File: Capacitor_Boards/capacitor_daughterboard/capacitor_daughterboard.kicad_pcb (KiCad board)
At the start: 2 copper layers, 33 x 32 mm, 5 parts, among them P1 Conn_01x02_Male, P2 Conn_01x02_Male

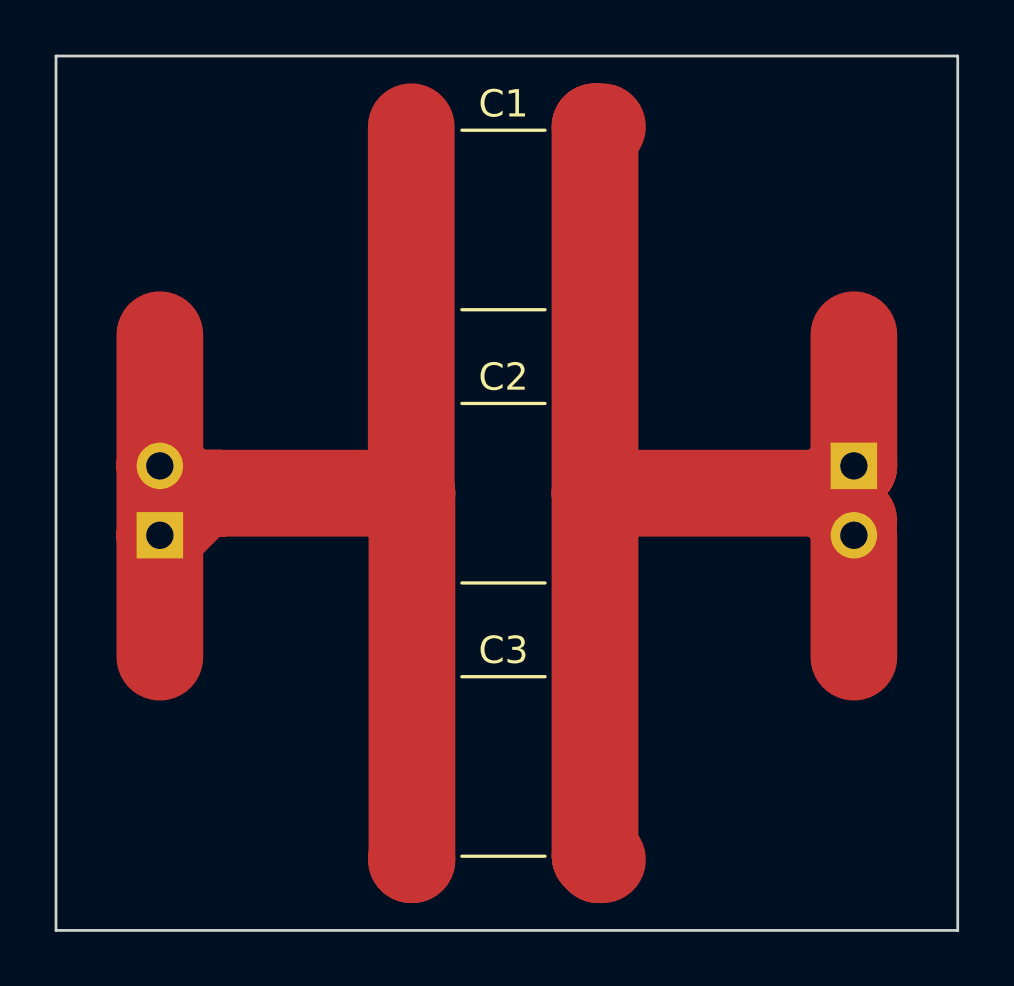
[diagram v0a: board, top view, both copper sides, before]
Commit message: resized capacitor daughterboard to have just 2 caps.
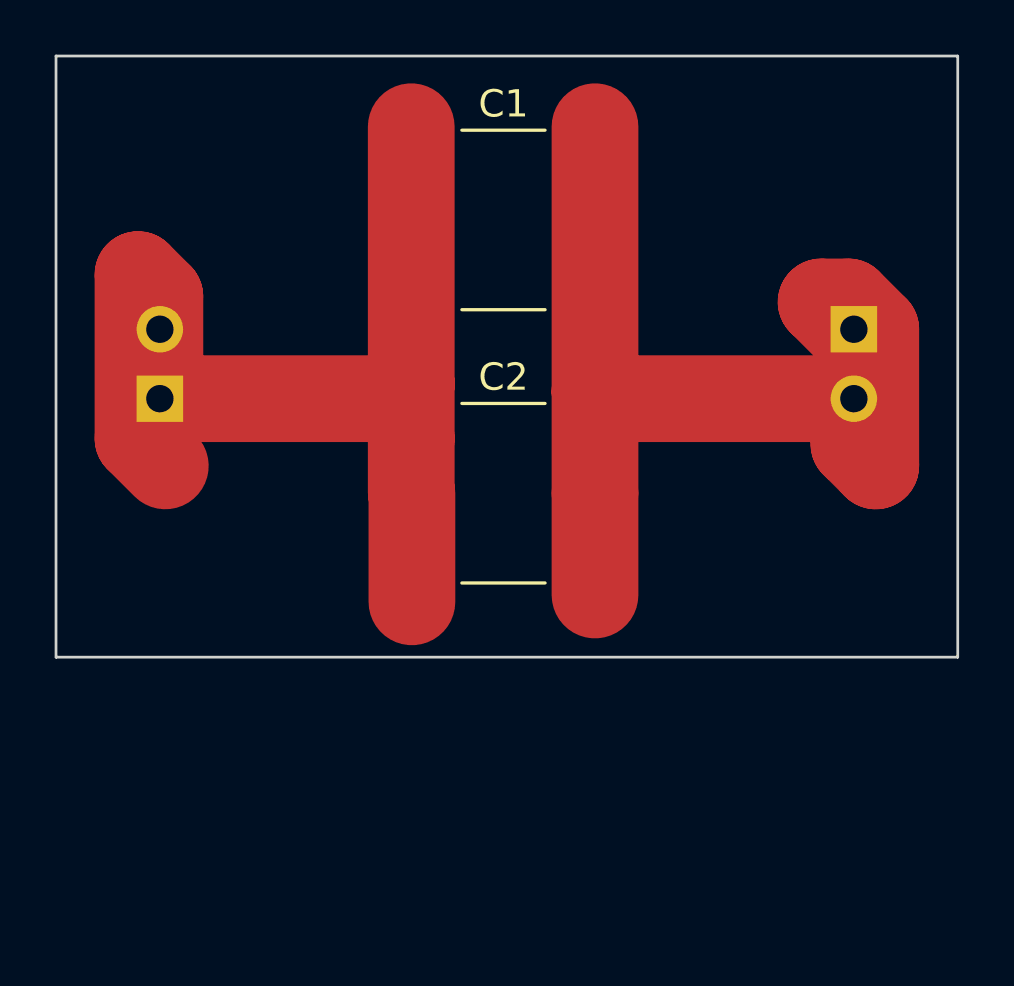
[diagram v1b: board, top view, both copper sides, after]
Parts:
- removed C3: C, Capacitor_SMD:C_2225_5664Metric_Pad1.80x6.60mm_HandSolder
- moved J1 5.00 mm to (127.8, 81.5)
- moved J2 5.00 mm to (153.2, 79.0)
- renumbered P1 to J1, P2 to J2
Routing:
- net Net-(C1-Pad1): track 53.1 -> 39.1 mm
- net Net-(C1-Pad2): track 47.9 -> 38.5 mm
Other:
- board size 33 x 32 mm -> 33 x 22 mm
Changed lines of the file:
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@@
   (net 2 "Net-(C1-Pad2)")
-  (footprint "Capacitor_SMD:C_2225_5664Metric_Pad1.80x6.60mm_HandSolder" (layer "F.Cu")
-    (at 140.375 95)
-    (descr "Capacitor SMD 2225 (5664 Metric), square (rectangular) end terminal, IPC_7351 nominal with elongated pad for handsoldering. (Body size from: http://datasheets.avx.com/AVX-HV_MLCC.pdf), generated with kicad-footprint-generator")
-    (tags "capacitor handsolder")
-    (property "Sheetfile" "capacitor_daughterboard.kicad_sch")
-    (property "Sheetname" "")
-    (attr smd)
-    (fp_text reference "C3" (at 0 -4.25) (layer "F.SilkS")
-      (effects (font (size 1 1) (thickness 0.15)))
-    )
-    (fp_text value "C" (at 0 4.25) (layer "F.Fab")
-      (effects (font (size 1 1) (thickness 0.15)))
-    )
-    (fp_text user "${REFERENCE}" (at 0 0) (layer "F.Fab")
-      (effects (font (size 1 1) (thickness 0.15)))
-    )
-    (fp_line (start -1.522369 -3.285) (end 1.522369 -3.285) (layer "F.SilkS") (width 0.12))
-    (fp_line (start -1.522369 3.285) (end 1.522369 3.285) (layer "F.SilkS") (width 0.12))
-    (fp_line (start 3.78 3.55) (end -3.78 3.55) (layer "F.CrtYd") (width 0.05))
-    (fp_line (start -3.78 -3.55) (end 3.78 -3.55) (layer "F.CrtYd") (width 0.05))
-    (fp_line (start 3.78 -3.55) (end 3.78 3.55) (layer "F.CrtYd") (width 0.05))
-    (fp_line (start -3.78 3.55) (end -3.78 -3.55) (layer "F.CrtYd") (width 0.05))
-    (fp_line (start 2.86 -3.175) (end 2.86 3.175) (layer "F.Fab") (width 0.1))
-    (fp_line (start 2.86 3.175) (end -2.86 3.175) (layer "F.Fab") (width 0.1))
-    (fp_line (start -2.86 3.175) (end -2.86 -3.175) (layer "F.Fab") (width 0.1))
-    (fp_line (start -2.86 -3.175) (end 2.86 -3.175) (layer "F.Fab") (width 0.1))
-    (pad "1" smd roundrect (at -3.35 0) (size 2.8 7) (layers "F.Cu" "F.Paste" "F.Mask") (roundrect_rratio 0.138889)
-      (net 1 "Net-(C1-Pad1)") (pintype "passive"))
-    (pad "2" smd roundrect (at 3.35 0) (size 2.8 7) (layers "F.Cu" "F.Paste" "F.Mask") (roundrect_rratio 0.138889)
-      (net 2 "Net-(C1-Pad2)") (pintype "passive"))
-    (model "${KICAD6_3DMODEL_DIR}/Capacitor_SMD.3dshapes/C_2225_5664Metric.wrl"
-      (offset (xyz 0 0 0))
-      (scale (xyz 1 1 1))
-      (rotate (xyz 0 0 0))
-    )
-  )
   (footprint "Capacitor_SMD:C_2225_5664Metric_Pad1.80x6.60mm_HandSolder" (layer "F.Cu")
     (at 140.375 85)
@@
   )
   (footprint "Connector_PinHeader_2.54mm:PinHeader_1x02_P2.54mm_Vertical" (layer "B.Cu")
-    (at 153.19939 84 180)
+    (at 153.19939 79 180)
     (descr "Through hole straight pin header, 1x02, 2.54mm pitch, single row")
     (tags "Through hole pin header THT 1x02 2.54mm single row")
@@
     (property "Sheetname" "")
     (attr through_hole)
-    (fp_text reference "P2" (at 0 -5) (layer "B.SilkS")
+    (fp_text reference "J2" (at 0 -5) (layer "B.SilkS")
       (effects (font (size 1 1) (thickness 0.15)) (justify mirror))
     )
@@
   )
   (footprint "Connector_PinHeader_2.54mm:PinHeader_1x02_P2.54mm_Vertical" (layer "B.Cu")
-    (at 127.80061 86.54)
+    (at 127.80061 81.54)
     (descr "Through hole straight pin header, 1x02, 2.54mm pitch, single row")
     (tags "Through hole pin header THT 1x02 2.54mm single row")
@@
     (property "Sheetname" "")
     (attr through_hole)
-    (fp_text reference "P1" (at 0 2.33) (layer "B.SilkS")
+    (fp_text reference "J1" (at 0 2.33) (layer "B.SilkS")
       (effects (font (size 1 1) (thickness 0.15)) (justify mirror))
     )
@@
     )
   )
-  (gr_rect (start 124 69) (end 157 101) (layer "Edge.Cuts") (width 0.1) (fill none))
-  (segment (start 127.80061 86.54) (end 127.80061 84) (width 3.175) (layer "F.Cu") (net 1))
-  (segment (start 130 85) (end 128 85) (width 3.175) (layer "F.Cu") (net 1))
-  (segment (start 137.025 98.41248) (end 137 98.41248) (width 3.175) (layer "F.Cu") (net 1))
-  (segment (start 130 85) (end 129.34061 85) (width 3.175) (layer "F.Cu") (net 1))
-  (segment (start 137 84.975) (end 137.025 85) (width 3.175) (layer "F.Cu") (net 1))
-  (segment (start 127.80061 86.54) (end 127.80061 91) (width 3.175) (layer "F.Cu") (net 1))
-  (segment (start 127.80061 84) (end 127.80061 79.19939) (width 3.175) (layer "F.Cu") (net 1))
-  (segment (start 128.80061 85) (end 127.80061 84) (width 3.175) (layer "F.Cu") (net 1))
-  (segment (start 130 85) (end 137.025 85) (width 3.175) (layer "F.Cu") (net 1))
-  (segment (start 129.34061 85) (end 127.80061 86.54) (width 3.175) (layer "F.Cu") (net 1))
-  (segment (start 130 85) (end 128.80061 85) (width 3.175) (layer "F.Cu") (net 1))
-  (segment (start 137.025 85) (end 137.025 98.41248) (width 3.175) (layer "F.Cu") (net 1))
-  (segment (start 137 71.58752) (end 137 84.975) (width 3.175) (layer "F.Cu") (net 1))
-  (segment (start 143.725 85) (end 143.725 98.275) (width 3.175) (layer "F.Cu") (net 2))
-  (segment (start 153.19939 86.54) (end 153.19939 91) (width 3.175) (layer "F.Cu") (net 2))
-  (segment (start 143.86248 98.41248) (end 144 98.41248) (width 3.175) (layer "F.Cu") (net 2))
-  (segment (start 152.19939 85) (end 153.19939 86) (width 3.175) (layer "F.Cu") (net 2))
-  (segment (start 152.19939 85) (end 153.19939 84) (width 3.175) (layer "F.Cu") (net 2))
-  (segment (start 153.19939 79.19939) (end 153.19939 84) (width 3.175) (layer "F.Cu") (net 2))
-  (segment (start 143.725 85) (end 143.725 71.58752) (width 3.175) (layer "F.Cu") (net 2))
-  (segment (start 143.725 98.275) (end 143.86248 98.41248) (width 3.175) (layer "F.Cu") (net 2))
-  (segment (start 143.725 71.58752) (end 144 71.58752) (width 3.175) (layer "F.Cu") (net 2))
-  (segment (start 152.19939 85) (end 143.725 85) (width 3.175) (layer "F.Cu") (net 2))
+  (gr_rect (start 124 69) (end 157 91) (layer "Edge.Cuts") (width 0.1) (fill none))
+  (segment (start 137 83) (end 137 84.975) (width 3.175) (layer "F.Cu") (net 1))
+  (segment (start 137 81) (end 137 83) (width 3.175) (layer "F.Cu") (net 1))
+  (segment (start 127 83) (end 128 84) (width 3.175) (layer "F.Cu") (net 1))
+  (segment (start 127 77) (end 127 83) (width 3.175) (layer "F.Cu") (net 1))
+  (segment (start 137 71.58752) (end 137 81) (width 3.175) (layer "F.Cu") (net 1))
+  (segment (start 127.80061 81.54) (end 136.46 81.54) (width 3.175) (layer "F.Cu") (net 1))
+  (segment (start 137.025 85) (end 137.025 88.975) (width 3.175) (layer "F.Cu") (net 1))
+  (segment (start 127.80061 77.80061) (end 127 77) (width 3.175) (layer "F.Cu") (net 1))
+  (segment (start 127.80061 81.54) (end 127.80061 77.80061) (width 3.175) (layer "F.Cu") (net 1))
+  (segment (start 136.46 81.54) (end 137 81) (width 3.175) (layer "F.Cu") (net 1))
+  (segment (start 154 84) (end 154 79) (width 3.175) (layer "F.Cu") (net 2))
+  (segment (start 153.19939 81.54) (end 143.99 81.54) (width 3.175) (layer "F.Cu") (net 2))
+  (segment (start 153 78) (end 154 79) (width 3.175) (layer "F.Cu") (net 2))
+  (segment (start 143.725 85) (end 143.725 88.725) (width 3.175) (layer "F.Cu") (net 2))
+  (segment (start 153.19939 83.19939) (end 154 84) (width 3.175) (layer "F.Cu") (net 2))
+  (segment (start 153.19939 79) (end 153 79) (width 3.175) (layer "F.Cu") (net 2))
+  (segment (start 153 79) (end 152 78) (width 3.175) (layer "F.Cu") (net 2))
+  (segment (start 143.725 85) (end 143.725 81.275) (width 3.175) (layer "F.Cu") (net 2))
+  (segment (start 153.19939 81.54) (end 153.19939 83.19939) (width 3.175) (layer "F.Cu") (net 2))
+  (segment (start 143.725 81.275) (end 143.725 71.58752) (width 3.175) (layer "F.Cu") (net 2))
+  (segment (start 152 78) (end 153 78) (width 3.175) (layer "F.Cu") (net 2))
+  (segment (start 143.99 81.54) (end 143.725 81.275) (width 3.175) (layer "F.Cu") (net 2))
 )

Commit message: Connected the QLA  connector
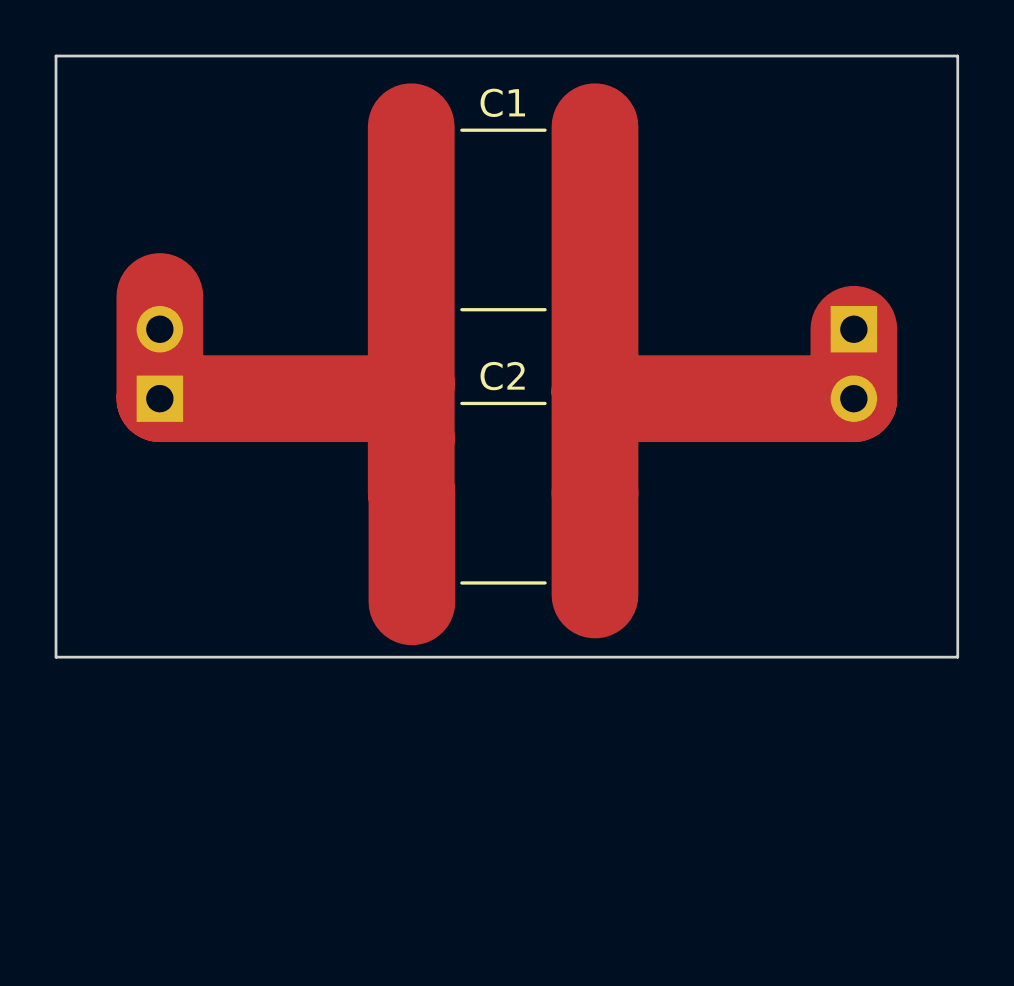
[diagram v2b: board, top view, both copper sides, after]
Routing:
- net Net-(C1-Pad2): track 38.5 -> 29.3 mm
- net Net-(C1-Pad1): track 39.1 -> 30.5 mm
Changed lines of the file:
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@@
   (segment (start 137 83) (end 137 84.975) (width 3.175) (layer "F.Cu") (net 1))
   (segment (start 137 81) (end 137 83) (width 3.175) (layer "F.Cu") (net 1))
-  (segment (start 127 83) (end 128 84) (width 3.175) (layer "F.Cu") (net 1))
-  (segment (start 127 77) (end 127 83) (width 3.175) (layer "F.Cu") (net 1))
   (segment (start 137 71.58752) (end 137 81) (width 3.175) (layer "F.Cu") (net 1))
   (segment (start 127.80061 81.54) (end 136.46 81.54) (width 3.175) (layer "F.Cu") (net 1))
   (segment (start 137.025 85) (end 137.025 88.975) (width 3.175) (layer "F.Cu") (net 1))
-  (segment (start 127.80061 77.80061) (end 127 77) (width 3.175) (layer "F.Cu") (net 1))
   (segment (start 127.80061 81.54) (end 127.80061 77.80061) (width 3.175) (layer "F.Cu") (net 1))
   (segment (start 136.46 81.54) (end 137 81) (width 3.175) (layer "F.Cu") (net 1))
-  (segment (start 154 84) (end 154 79) (width 3.175) (layer "F.Cu") (net 2))
   (segment (start 153.19939 81.54) (end 143.99 81.54) (width 3.175) (layer "F.Cu") (net 2))
-  (segment (start 153 78) (end 154 79) (width 3.175) (layer "F.Cu") (net 2))
   (segment (start 143.725 85) (end 143.725 88.725) (width 3.175) (layer "F.Cu") (net 2))
-  (segment (start 153.19939 83.19939) (end 154 84) (width 3.175) (layer "F.Cu") (net 2))
-  (segment (start 153.19939 79) (end 153 79) (width 3.175) (layer "F.Cu") (net 2))
-  (segment (start 153 79) (end 152 78) (width 3.175) (layer "F.Cu") (net 2))
   (segment (start 143.725 85) (end 143.725 81.275) (width 3.175) (layer "F.Cu") (net 2))
-  (segment (start 153.19939 81.54) (end 153.19939 83.19939) (width 3.175) (layer "F.Cu") (net 2))
   (segment (start 143.725 81.275) (end 143.725 71.58752) (width 3.175) (layer "F.Cu") (net 2))
-  (segment (start 152 78) (end 153 78) (width 3.175) (layer "F.Cu") (net 2))
   (segment (start 143.99 81.54) (end 143.725 81.275) (width 3.175) (layer "F.Cu") (net 2))
+  (segment (start 153.19939 81.54) (end 153.19939 79) (width 3.175) (layer "F.Cu") (net 2))
 )

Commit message: Shrunk Daughter Board
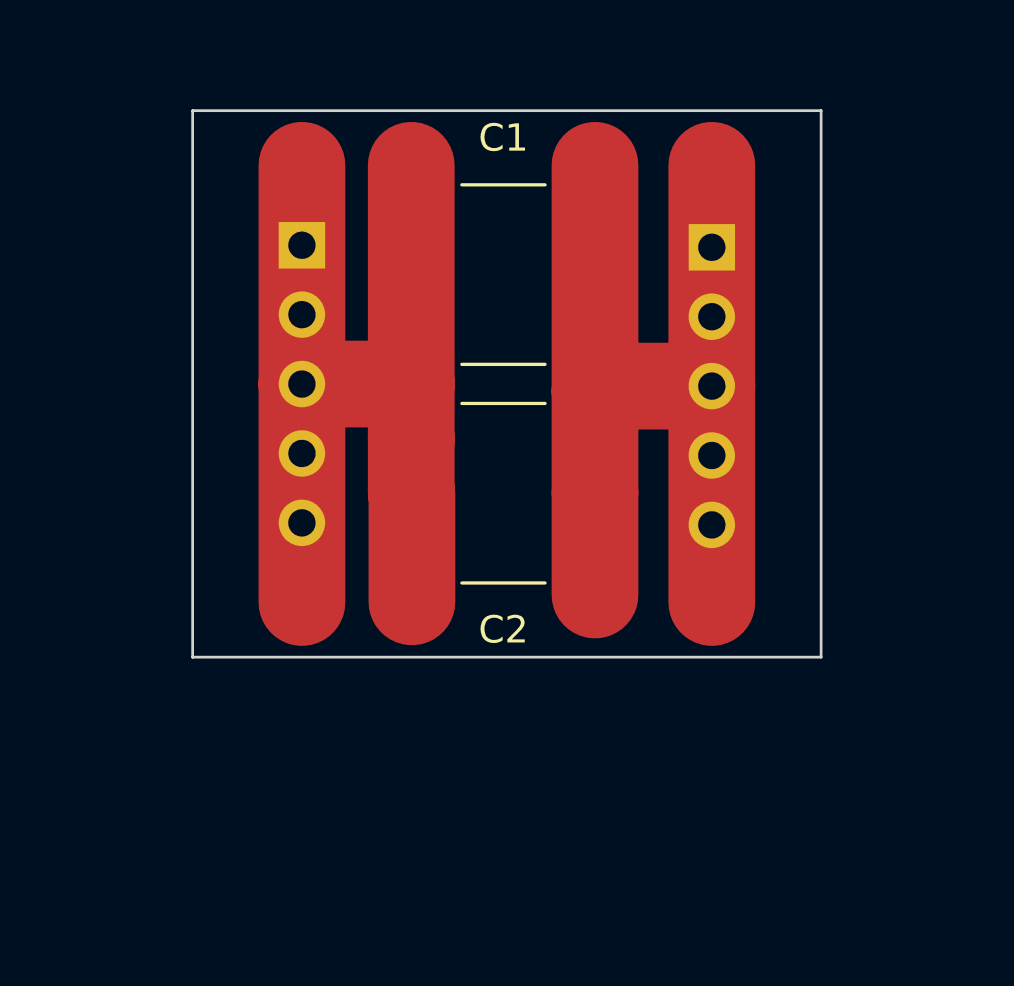
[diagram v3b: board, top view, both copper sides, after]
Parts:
- J1, J2: value Conn_01x02_Male -> Conn_01x05; footprint Connector_PinHeader_2.54mm:PinHeader_1x02_P2.54mm_Vertical -> Connector_PinHeader_2.54mm:PinHeader_1x05_P2.54mm_Vertical
- moved J1 7.65 mm to (133.0, 75.9), turned to 180 degrees
- moved J2 6.00 mm to (148.0, 76.0)
- moved C1 2.00 mm to (140.4, 77.0)
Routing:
- net Net-(C1-Pad2): track 29.3 -> 36.1 mm
- net Net-(C1-Pad1): track 30.5 -> 36.0 mm
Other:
- board size 33 x 22 mm -> 23 x 20 mm

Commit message: Single pad for caps.
Further reduced size of daughterboard.
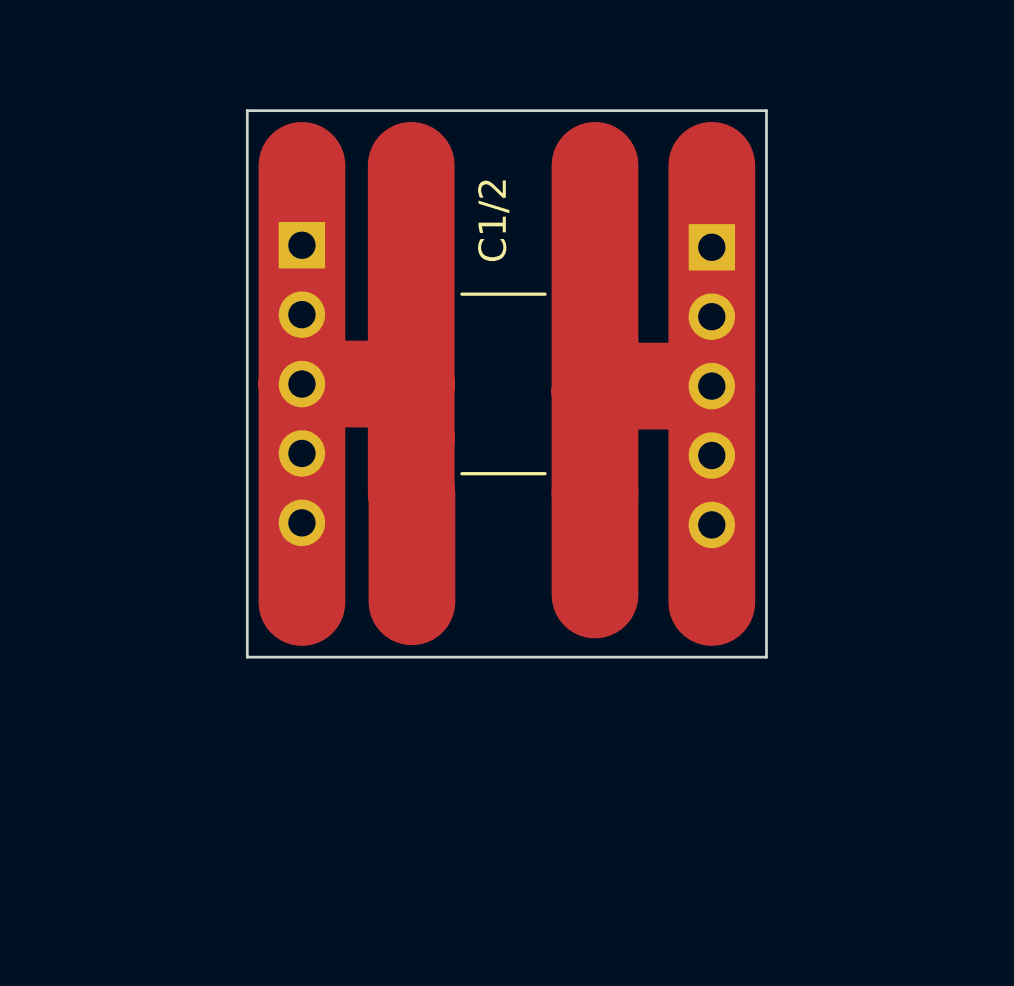
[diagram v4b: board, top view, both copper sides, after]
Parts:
- removed C2: C, Capacitor_SMD:C_2225_5664Metric_Pad1.80x6.60mm_HandSolder
- moved C1/2 4.00 mm to (140.4, 81.0)
- renumbered C1 to C1/2
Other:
- board size 23 x 20 mm -> 19 x 20 mm
